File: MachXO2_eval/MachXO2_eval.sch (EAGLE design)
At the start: 29 parts, among them U1 LCMXO2-256HC-4TG100C, U2 AE-FT2232, U3 XC6202P332TH

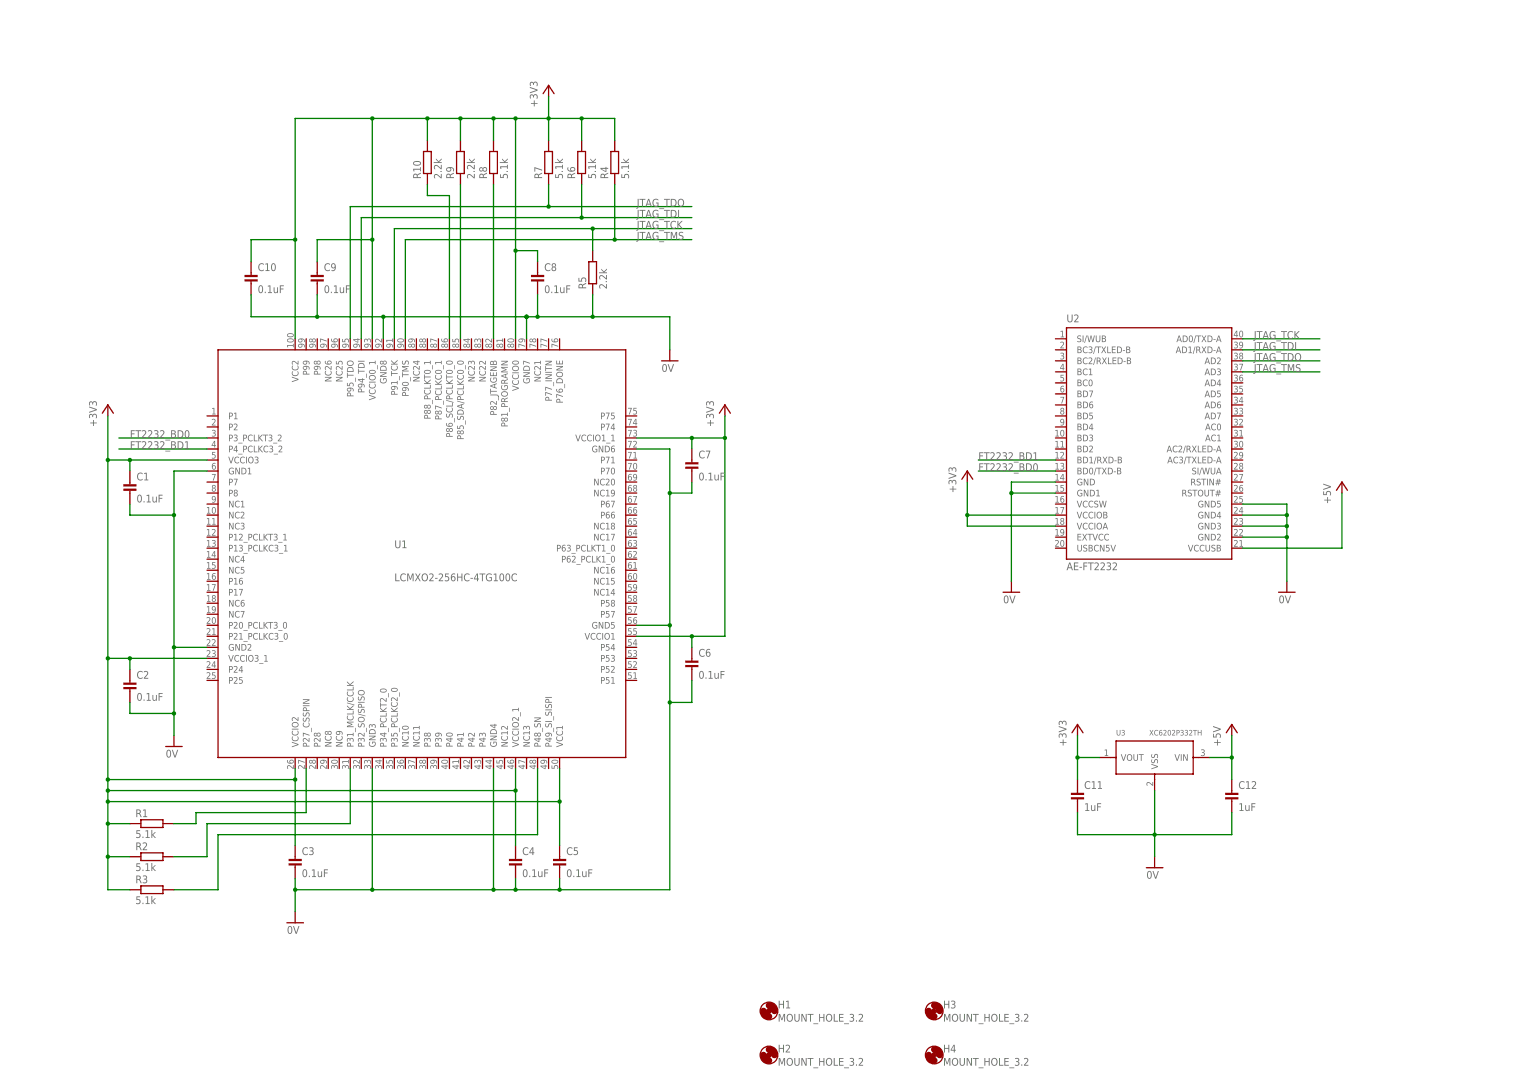
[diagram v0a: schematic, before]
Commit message: ピンを増設
・動作確認用のピンを基板外に出すための配線を追加
・外部電源コネクターとケミコンを追加
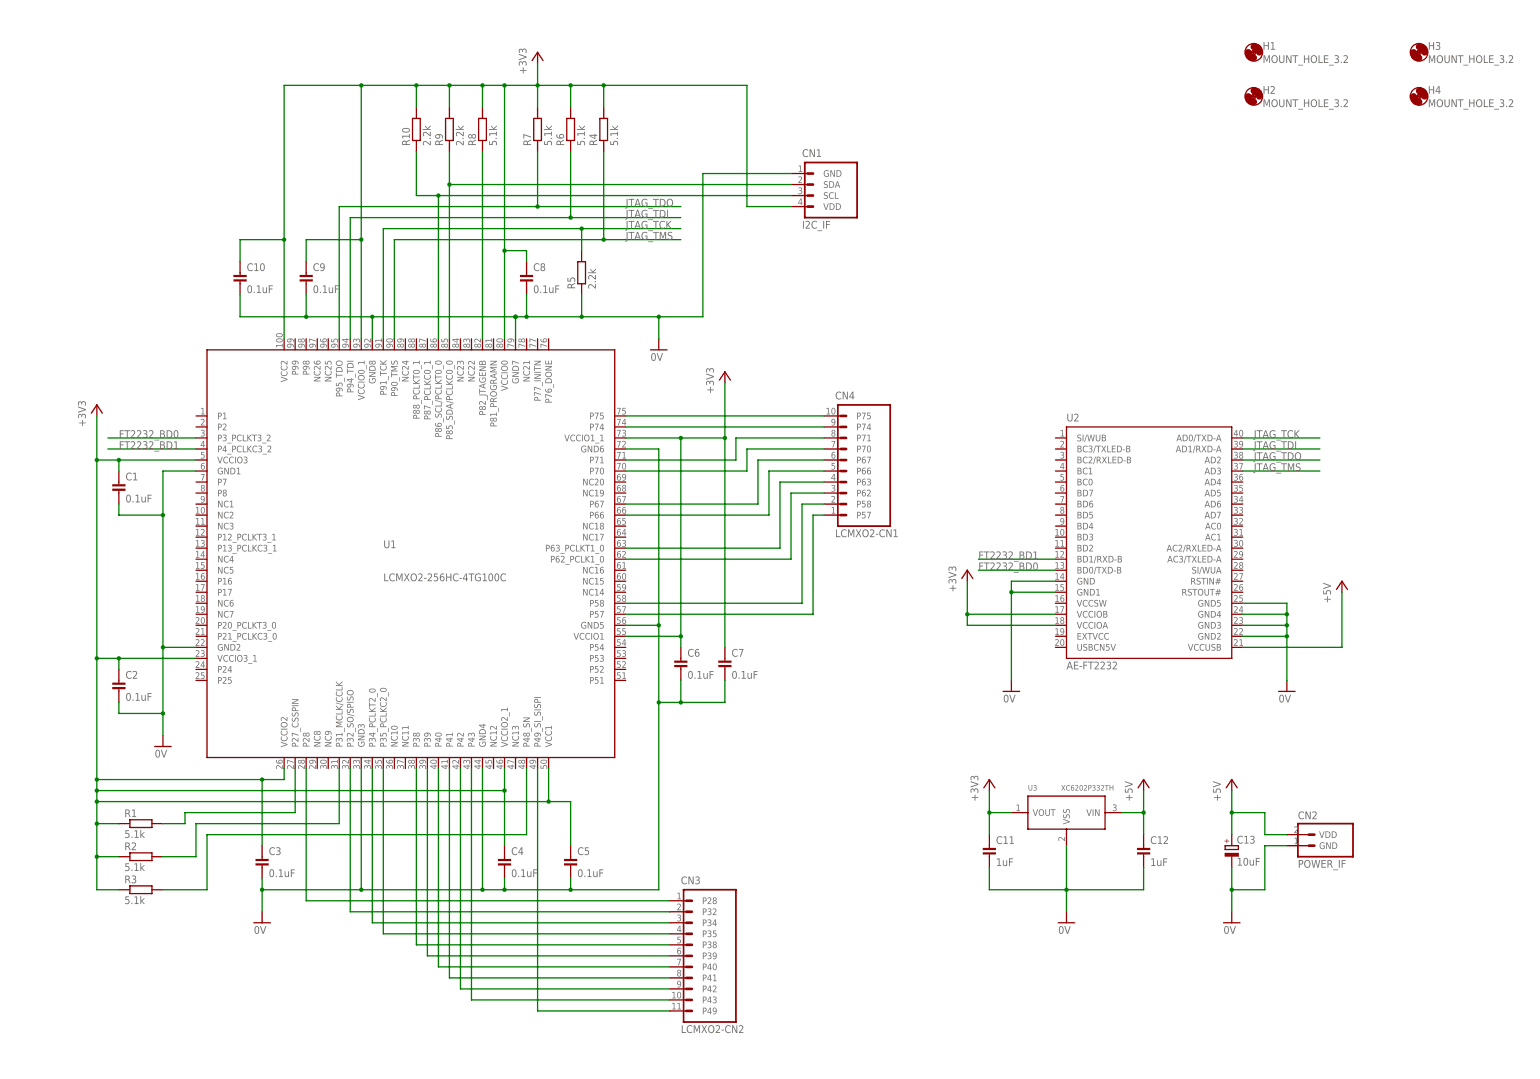
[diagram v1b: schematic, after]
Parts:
- added C13: 10uF, Parts:ELECAP_200MIL
- added CN1: I2C_IF, PartsForProto:I2C_IF
- added CN2: POWER_IF, PartsForProto:POWER_IF
- added CN3: LCMXO2-CN2, PartsForProto:LCMXO2-CN2
- added CN4: LCMXO2-CN1, PartsForProto:LCMXO2-CN1
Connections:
- new net N$11: CN4.P57, U1.P57
- new net N$12: CN4.P58, U1.P58
- new net N$13: CN4.P62, U1.P62_PCLK1_0
- new net N$17: CN3.P43, U1.P43
- new net N$18: CN3.P42, U1.P42
- new net N$19: CN3.P41, U1.P41
- new net N$20: CN3.P40, U1.P40
- new net N$21: CN3.P39, U1.P39
- new net N$22: CN3.P38, U1.P38
- new net N$23: CN3.P49, U1.P49_SI_SISPI
- new net N$24: CN3.P35, U1.P35_PCLKC2_0
- new net N$25: CN3.P34, U1.P34_PCLKT2_0
- new net N$26: CN3.P32, U1.P32_SO/SPISO
- new net N$27: CN3.P28, U1.P28
- new net N$28: CN4.P70, U1.P70
- new net N$29: CN4.P71, U1.P71
- new net N$4: CN4.P74, U1.P74
- new net N$5: CN4.P75, U1.P75
- new net N$6: CN4.P67, U1.P67
- new net N$7: CN4.P66, U1.P66
- new net N$9: CN4.P63, U1.P63_PCLKT1_0
- net +3V3: now also CN1.VDD
- net +5V: now also C13.+, CN2.VDD
- net 0V: now also C13.-, CN1.GND, CN2.GND
- net I2C_SCL: now also CN1.SCL
- net N$2: now also CN1.SDA
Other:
- moved on the sheet: C1, C10, C11, C12, C2, C3, C4, C5, C6, C7, C8, C9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

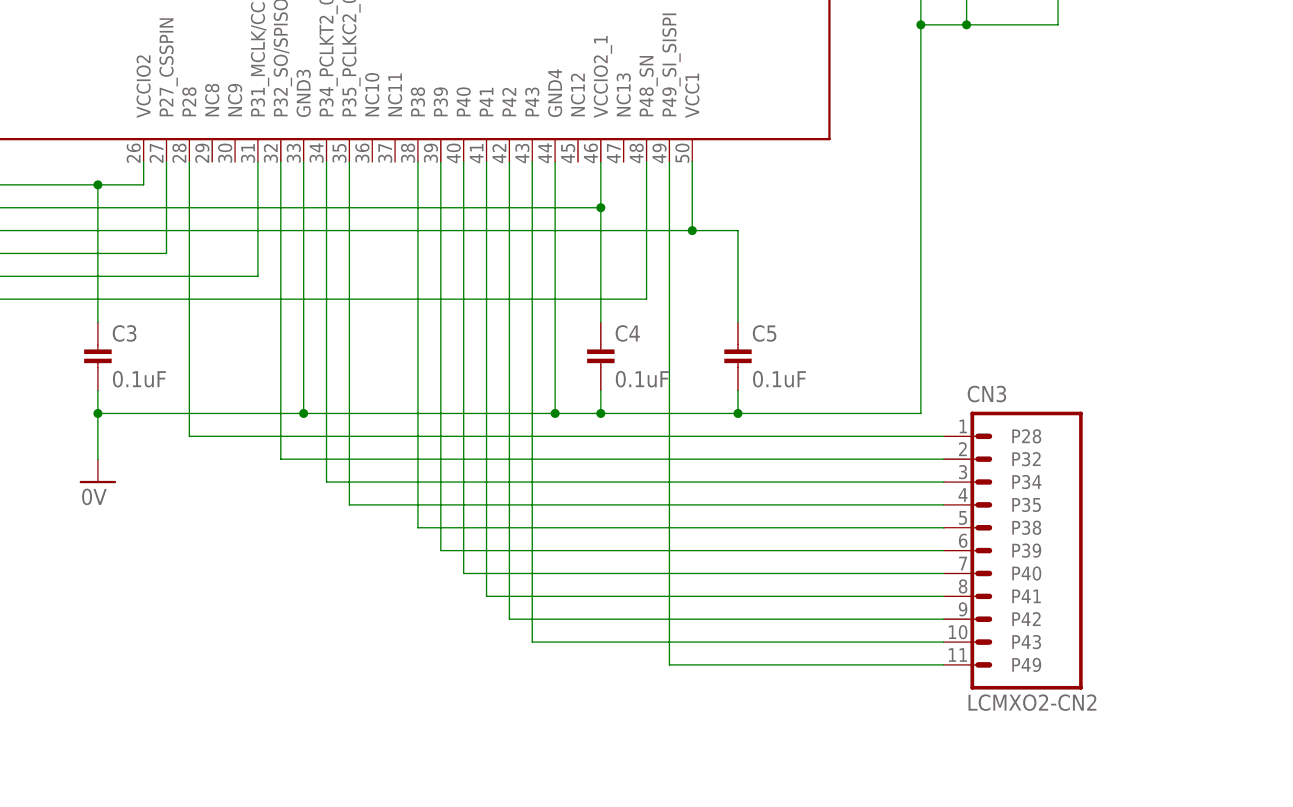
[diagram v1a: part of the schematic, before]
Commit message: MachXO2評価基板修正
外出しピンを追加
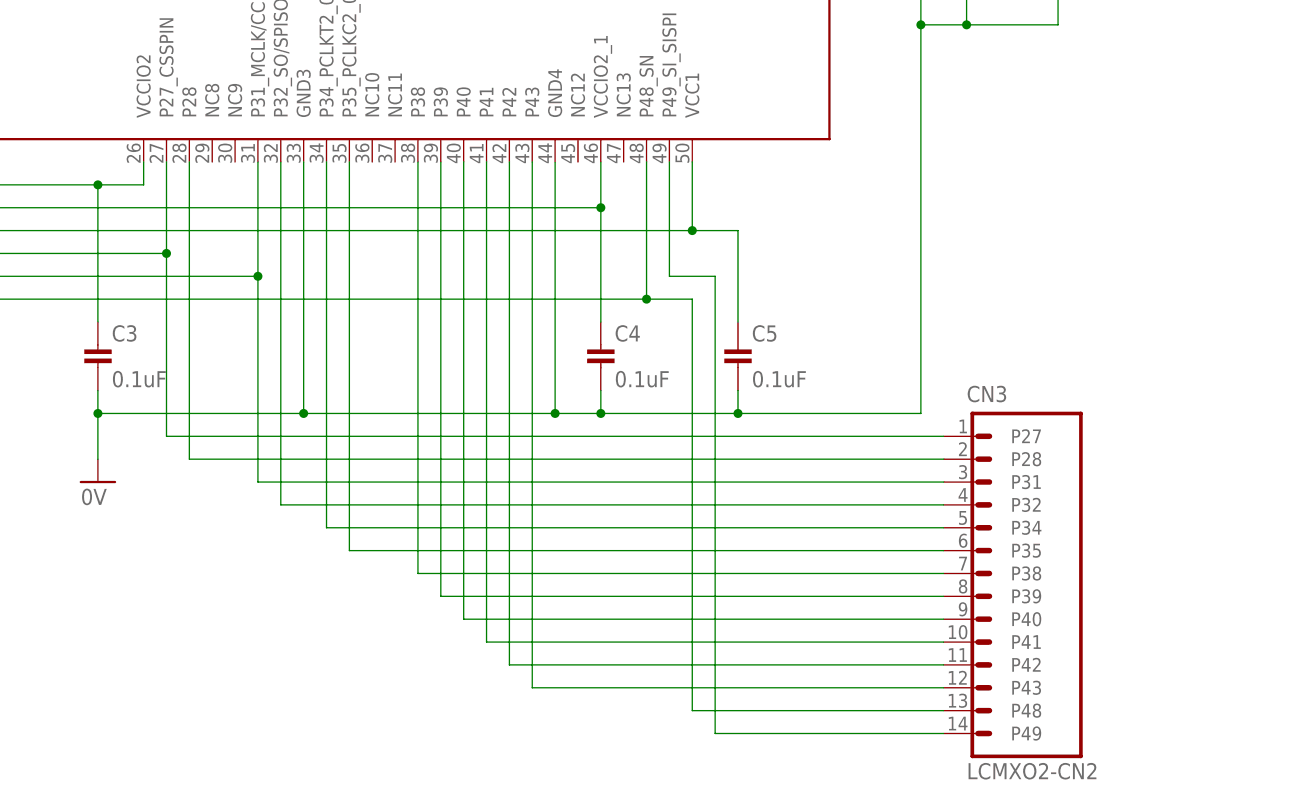
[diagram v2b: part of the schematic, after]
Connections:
- net N$10: now also CN3.P48
- net N$3: now also CN3.P27
- net N$8: now also CN3.P31
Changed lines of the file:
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@@
 <wire x1="68.58" y1="58.42" x2="68.58" y2="66.04" width="0.1524" layer="91"/>
 <wire x1="68.58" y1="66.04" x2="101.6" y2="66.04" width="0.1524" layer="91"/>
+<pinref part="CN3" gate="G$1" pin="P31"/>
+<wire x1="177.8" y1="43.18" x2="101.6" y2="43.18" width="0.1524" layer="91"/>
+<wire x1="101.6" y1="43.18" x2="101.6" y2="66.04" width="0.1524" layer="91"/>
+<junction x="101.6" y="66.04"/>
 </segment>
 </net>
@@
 <pinref part="U1" gate="G$1" pin="P48_SN"/>
 <wire x1="144.78" y1="78.74" x2="144.78" y2="63.5" width="0.1524" layer="91"/>
+<wire x1="144.78" y1="63.5" x2="149.86" y2="63.5" width="0.1524" layer="91"/>
+<junction x="144.78" y="63.5"/>
+<pinref part="CN3" gate="G$1" pin="P48"/>
+<wire x1="177.8" y1="17.78" x2="149.86" y2="17.78" width="0.1524" layer="91"/>
+<wire x1="149.86" y1="17.78" x2="149.86" y2="63.5" width="0.1524" layer="91"/>
 </segment>
 </net>
@@
 <pinref part="R1" gate="G$1" pin="2"/>
 <wire x1="66.04" y1="66.04" x2="60.96" y2="66.04" width="0.1524" layer="91"/>
+<wire x1="91.44" y1="68.58" x2="91.44" y2="48.26" width="0.1524" layer="91"/>
+<junction x="91.44" y="68.58"/>
+<pinref part="CN3" gate="G$1" pin="P27"/>
+<wire x1="91.44" y1="48.26" x2="177.8" y2="48.26" width="0.1524" layer="91"/>
 </segment>
 </net>
@@
 <segment>
 <pinref part="U1" gate="G$1" pin="P43"/>
+<wire x1="132.08" y1="20.32" x2="132.08" y2="78.74" width="0.1524" layer="91"/>
 <pinref part="CN3" gate="G$1" pin="P43"/>
-<wire x1="177.8" y1="25.4" x2="132.08" y2="25.4" width="0.1524" layer="91"/>
-<wire x1="132.08" y1="25.4" x2="132.08" y2="78.74" width="0.1524" layer="91"/>
+<wire x1="177.8" y1="20.32" x2="132.08" y2="20.32" width="0.1524" layer="91"/>
 </segment>
 </net>
@@
 <segment>
 <pinref part="U1" gate="G$1" pin="P42"/>
+<wire x1="129.54" y1="22.86" x2="129.54" y2="78.74" width="0.1524" layer="91"/>
 <pinref part="CN3" gate="G$1" pin="P42"/>
-<wire x1="177.8" y1="27.94" x2="129.54" y2="27.94" width="0.1524" layer="91"/>
-<wire x1="129.54" y1="27.94" x2="129.54" y2="78.74" width="0.1524" layer="91"/>
+<wire x1="177.8" y1="22.86" x2="129.54" y2="22.86" width="0.1524" layer="91"/>
 </segment>
 </net>
@@
 <segment>
 <pinref part="U1" gate="G$1" pin="P41"/>
-<wire x1="127" y1="78.74" x2="127" y2="30.48" width="0.1524" layer="91"/>
+<wire x1="127" y1="78.74" x2="127" y2="25.4" width="0.1524" layer="91"/>
 <pinref part="CN3" gate="G$1" pin="P41"/>
-<wire x1="177.8" y1="30.48" x2="127" y2="30.48" width="0.1524" layer="91"/>
+<wire x1="177.8" y1="25.4" x2="127" y2="25.4" width="0.1524" layer="91"/>
 </segment>
 </net>
@@
 <segment>
 <pinref part="U1" gate="G$1" pin="P40"/>
-<wire x1="124.46" y1="78.74" x2="124.46" y2="33.02" width="0.1524" layer="91"/>
+<wire x1="124.46" y1="78.74" x2="124.46" y2="27.94" width="0.1524" layer="91"/>
 <pinref part="CN3" gate="G$1" pin="P40"/>
-<wire x1="177.8" y1="33.02" x2="124.46" y2="33.02" width="0.1524" layer="91"/>
+<wire x1="177.8" y1="27.94" x2="124.46" y2="27.94" width="0.1524" layer="91"/>
 </segment>
 </net>
@@
 <segment>
 <pinref part="U1" gate="G$1" pin="P39"/>
-<wire x1="121.92" y1="78.74" x2="121.92" y2="35.56" width="0.1524" layer="91"/>
+<wire x1="121.92" y1="78.74" x2="121.92" y2="30.48" width="0.1524" layer="91"/>
 <pinref part="CN3" gate="G$1" pin="P39"/>
-<wire x1="177.8" y1="35.56" x2="121.92" y2="35.56" width="0.1524" layer="91"/>
+<wire x1="177.8" y1="30.48" x2="121.92" y2="30.48" width="0.1524" layer="91"/>
 </segment>
 </net>
@@
 <segment>
 <pinref part="U1" gate="G$1" pin="P38"/>
-<wire x1="119.38" y1="78.74" x2="119.38" y2="38.1" width="0.1524" layer="91"/>
+<wire x1="119.38" y1="78.74" x2="119.38" y2="33.02" width="0.1524" layer="91"/>
 <pinref part="CN3" gate="G$1" pin="P38"/>
-<wire x1="177.8" y1="38.1" x2="119.38" y2="38.1" width="0.1524" layer="91"/>
-</segment>
-</net>
-<net name="N$23" class="0">
-<segment>
-<pinref part="U1" gate="G$1" pin="P49_SI_SISPI"/>
-<pinref part="CN3" gate="G$1" pin="P49"/>
-<wire x1="177.8" y1="22.86" x2="147.32" y2="22.86" width="0.1524" layer="91"/>
-<wire x1="147.32" y1="22.86" x2="147.32" y2="78.74" width="0.1524" layer="91"/>
+<wire x1="177.8" y1="33.02" x2="119.38" y2="33.02" width="0.1524" layer="91"/>
 </segment>
 </net>
@@
 <segment>
 <pinref part="U1" gate="G$1" pin="P35_PCLKC2_0"/>
-<wire x1="111.76" y1="78.74" x2="111.76" y2="40.64" width="0.1524" layer="91"/>
+<wire x1="111.76" y1="78.74" x2="111.76" y2="35.56" width="0.1524" layer="91"/>
 <pinref part="CN3" gate="G$1" pin="P35"/>
-<wire x1="177.8" y1="40.64" x2="111.76" y2="40.64" width="0.1524" layer="91"/>
+<wire x1="177.8" y1="35.56" x2="111.76" y2="35.56" width="0.1524" layer="91"/>
 </segment>
 </net>
@@
 <segment>
 <pinref part="U1" gate="G$1" pin="P34_PCLKT2_0"/>
-<wire x1="109.22" y1="78.74" x2="109.22" y2="43.18" width="0.1524" layer="91"/>
+<wire x1="109.22" y1="78.74" x2="109.22" y2="38.1" width="0.1524" layer="91"/>
 <pinref part="CN3" gate="G$1" pin="P34"/>
-<wire x1="177.8" y1="43.18" x2="109.22" y2="43.18" width="0.1524" layer="91"/>
+<wire x1="177.8" y1="38.1" x2="109.22" y2="38.1" width="0.1524" layer="91"/>
 </segment>
 </net>
@@
 <segment>
 <pinref part="U1" gate="G$1" pin="P32_SO/SPISO"/>
-<wire x1="104.14" y1="78.74" x2="104.14" y2="45.72" width="0.1524" layer="91"/>
+<wire x1="104.14" y1="78.74" x2="104.14" y2="40.64" width="0.1524" layer="91"/>
 <pinref part="CN3" gate="G$1" pin="P32"/>
-<wire x1="177.8" y1="45.72" x2="104.14" y2="45.72" width="0.1524" layer="91"/>
+<wire x1="177.8" y1="40.64" x2="104.14" y2="40.64" width="0.1524" layer="91"/>
 </segment>
 </net>
@@
 <segment>
 <pinref part="U1" gate="G$1" pin="P28"/>
-<wire x1="93.98" y1="78.74" x2="93.98" y2="48.26" width="0.1524" layer="91"/>
+<wire x1="93.98" y1="78.74" x2="93.98" y2="45.72" width="0.1524" layer="91"/>
 <pinref part="CN3" gate="G$1" pin="P28"/>
-<wire x1="177.8" y1="48.26" x2="93.98" y2="48.26" width="0.1524" layer="91"/>
+<wire x1="177.8" y1="45.72" x2="93.98" y2="45.72" width="0.1524" layer="91"/>
 </segment>
 </net>
@@
 </segment>
 </net>
+<net name="N$14" class="0">
+<segment>
+<pinref part="CN3" gate="G$1" pin="P49"/>
+<wire x1="177.8" y1="15.24" x2="152.4" y2="15.24" width="0.1524" layer="91"/>
+<wire x1="152.4" y1="15.24" x2="152.4" y2="66.04" width="0.1524" layer="91"/>
+<pinref part="U1" gate="G$1" pin="P49_SI_SISPI"/>
+<wire x1="152.4" y1="66.04" x2="147.32" y2="66.04" width="0.1524" layer="91"/>
+<wire x1="147.32" y1="66.04" x2="147.32" y2="78.74" width="0.1524" layer="91"/>
+</segment>
+</net>
